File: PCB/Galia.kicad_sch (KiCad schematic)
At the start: 9 parts, among them J1 USB In, J2 USB, SW1 Bootsel, SW2 Reset, U2 TPD4E05U06

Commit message: Changed PTS645 LCSC part number
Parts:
- SW1, SW2: LCSC C285466 -> C285487
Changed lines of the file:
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@@
       (effects (font (size 1.27 1.27)) hide)
     )
-    (property "LCSC" "C285466" (at 134.62 27.94 0)
+    (property "LCSC" "C285487" (at 134.62 27.94 0)
       (effects (font (size 1.27 1.27)) hide)
     )
@@
       (effects (font (size 1.27 1.27)) hide)
     )
-    (property "LCSC" "C285466" (at 134.62 40.64 0)
+    (property "LCSC" "C285487" (at 134.62 40.64 0)
       (effects (font (size 1.27 1.27)) hide)
     )

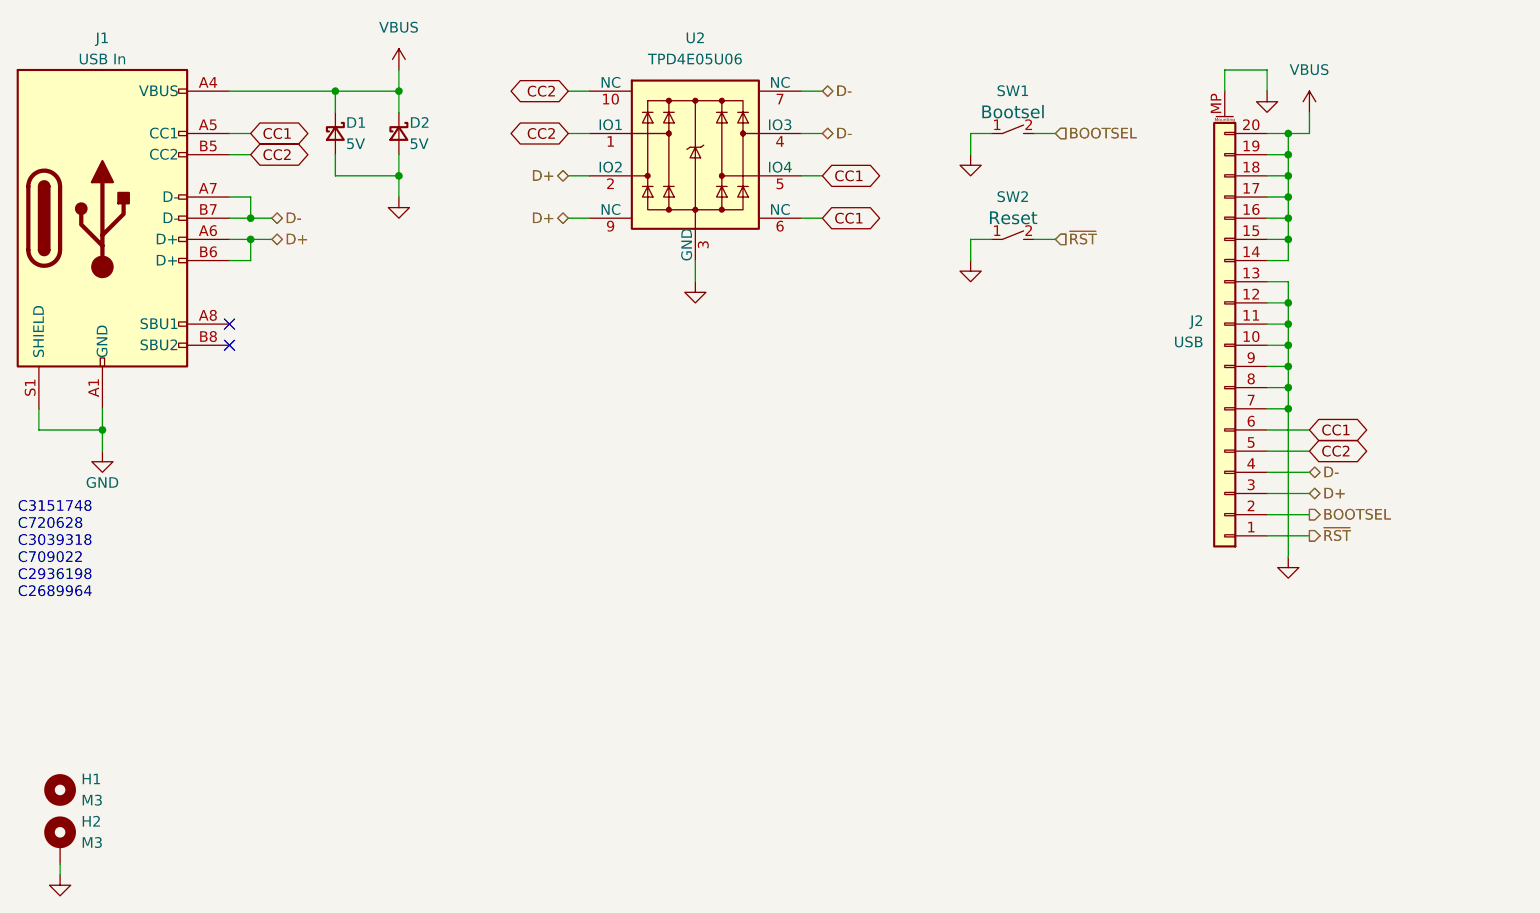
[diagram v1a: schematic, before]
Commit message: 17/07/2023 update
Changed 20 pin FFC connector to 14 pin JST SH connector. Repositioned components.
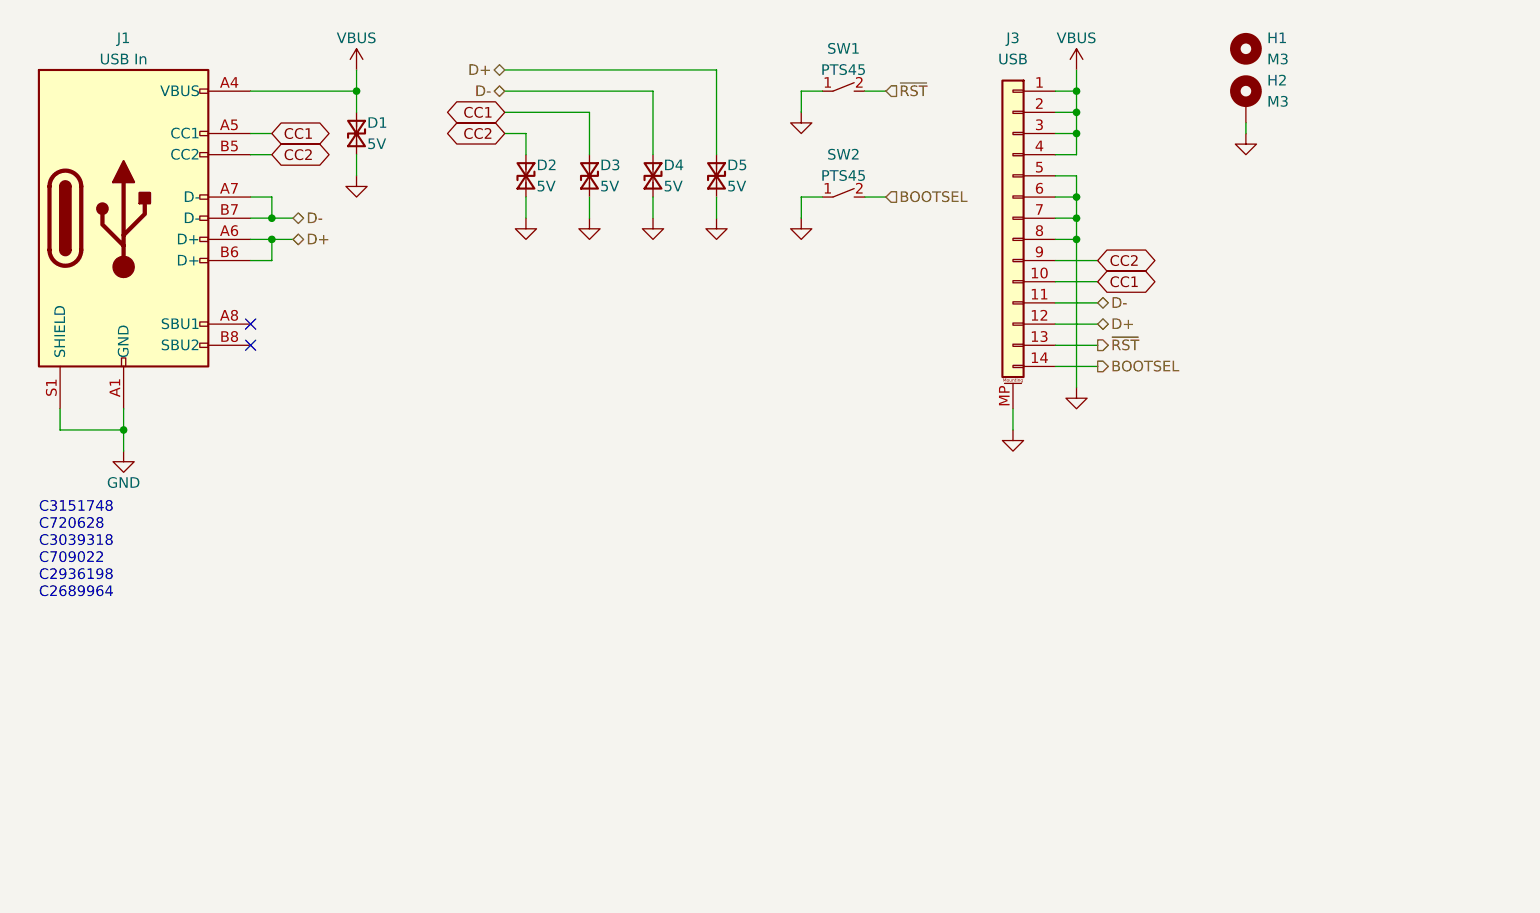
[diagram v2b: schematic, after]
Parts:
- removed D2: 5V, Diode_SMD:D_SOD-523, symbol Device:D_Schottky_Small
- removed J2: USB, Galia:HRS_FH34SRJ-20S-0.5SH(50), symbol Connector_Generic_MountingPin:Conn_01x20_MountingPin
- removed U2: TPD4E05U06, Galia:USON-10_2.5x1.0mm_P0.5mm, symbol Galia:TPD4E05U06
- added D2, D3, D4, D5: 5V, Galia:Texas_DPY0002A_0.6x1mm_P0.65mm, symbol Galia:D_TVS_Small
- added J3: USB, Galia:JST_SH_SM14B-SRSS-TB_1x14-1MP_P1.00mm_Horizontal, symbol Connector_Generic_MountingPin:Conn_01x14_MountingPin
- D1: symbol Device:D_Schottky_Small -> Galia:D_TVS_Small; LCSC C502546 -> C85708
- SW1: value Bootsel -> PTS45
- SW2: value Reset -> PTS45
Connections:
- net BOOTSEL: now also SW2.2 (B), J3.14 (Pin_14); no longer SW1.2 (B)
- net CC1: now also D3.1 (K), J3.10 (Pin_10)
- net CC2: now also D2.1 (K), J3.9 (Pin_9)
- net D+: now also D5.1 (K), J3.12 (Pin_12)
- net D-: now also D4.1 (K), J3.11 (Pin_11)
- net GND: now also D2.2 (A), D3.2 (A), D4.2 (A), D5.2 (A), J3.5 (Pin_5), J3.6 (Pin_6), J3.7 (Pin_7), J3.8 (Pin_8), J3.MP (MountPin)
- net VBUS: now also J3.1 (Pin_1), J3.2 (Pin_2), J3.3 (Pin_3), J3.4 (Pin_4)
- net ~{RST}: now also SW1.2 (B), J3.13 (Pin_13); no longer SW2.2 (B)
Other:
- moved on the sheet: H1, H2, J1, SW1, SW2

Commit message: 18/07/2023 update.
Changed JST connector back to 20 pin FFC. Centered connector.
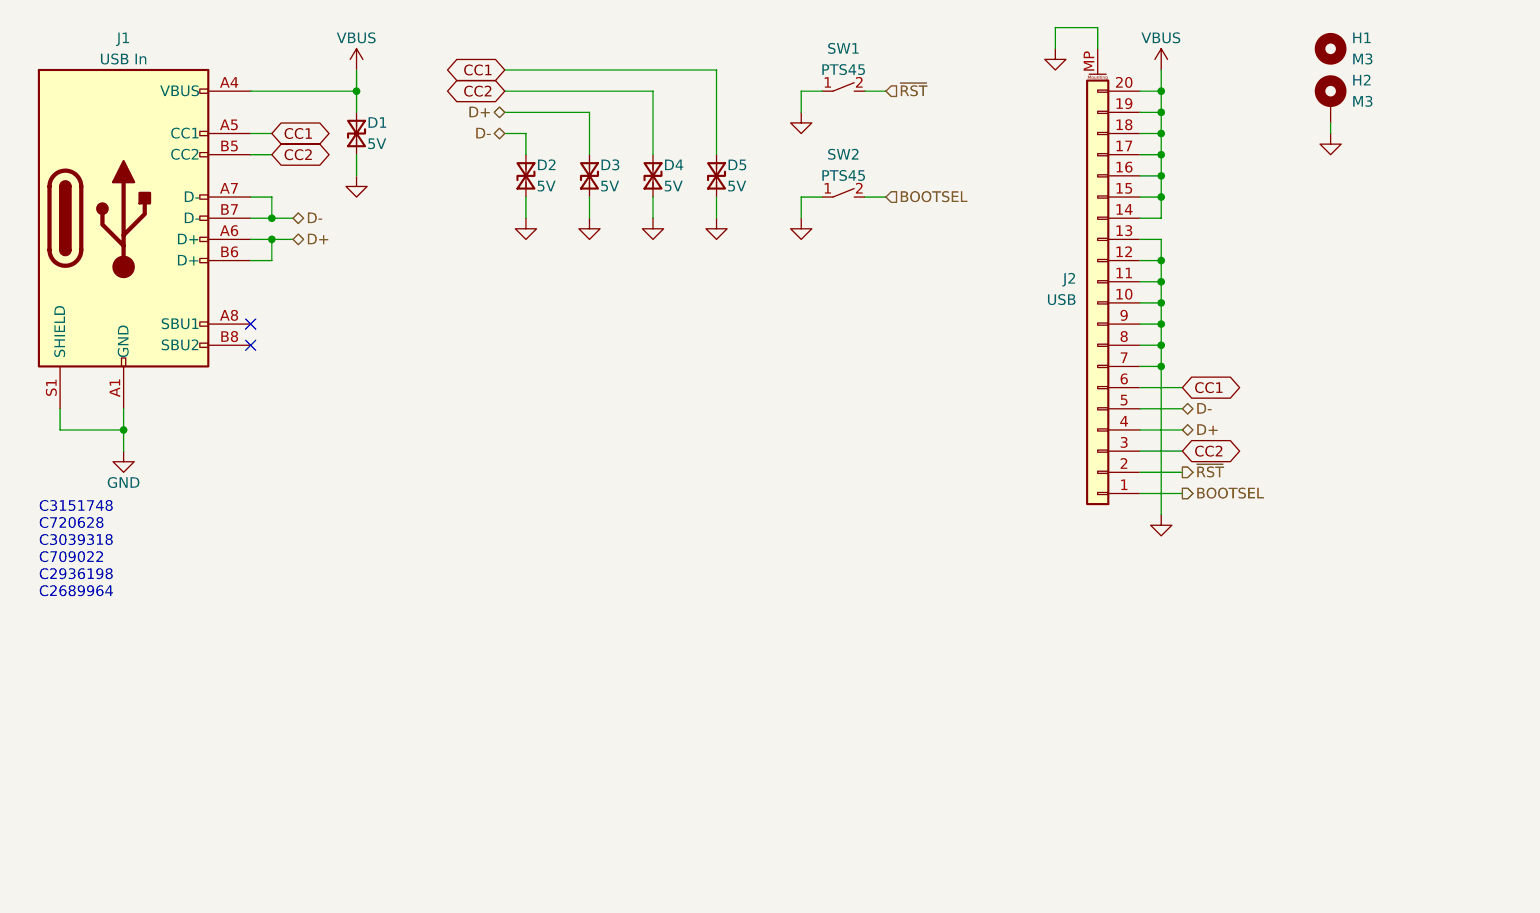
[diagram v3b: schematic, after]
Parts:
- removed J3: USB, Galia:JST_SH_SM14B-SRSS-TB_1x14-1MP_P1.00mm_Horizontal, symbol Connector_Generic_MountingPin:Conn_01x14_MountingPin
- added J2: USB, Galia:HRS_FH34SRJ-20S-0.5SH(50), symbol Connector_Generic_MountingPin:Conn_01x20_MountingPin
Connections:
- net BOOTSEL: now also J2.1 (Pin_1)
- net CC1: now also D5.1 (K), J2.6 (Pin_6); no longer D3.1 (K)
- net CC2: now also D4.1 (K), J2.3 (Pin_3); no longer D2.1 (K)
- net D+: now also D3.1 (K), J2.4 (Pin_4); no longer D5.1 (K)
- net D-: now also D2.1 (K), J2.5 (Pin_5); no longer D4.1 (K)
- net GND: now also J2.10 (Pin_10), J2.11 (Pin_11), J2.12 (Pin_12), J2.13 (Pin_13), J2.7 (Pin_7), J2.8 (Pin_8), J2.9 (Pin_9), J2.MP (MountPin)
- net VBUS: now also J2.14 (Pin_14), J2.15 (Pin_15), J2.16 (Pin_16), J2.17 (Pin_17), J2.18 (Pin_18), J2.19 (Pin_19), J2.20 (Pin_20)
- net ~{RST}: now also J2.2 (Pin_2)
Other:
- moved on the sheet: H1, H2

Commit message: Added LCSC part number.
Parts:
- J2: LCSC (none) -> C2802370
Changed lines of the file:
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@@
+      (effects (font (size 1.27 1.27)) hide)
+    )
+    (property "LCSC" "C2802370" (at 144.78 48.26 0)
       (effects (font (size 1.27 1.27)) hide)
     )

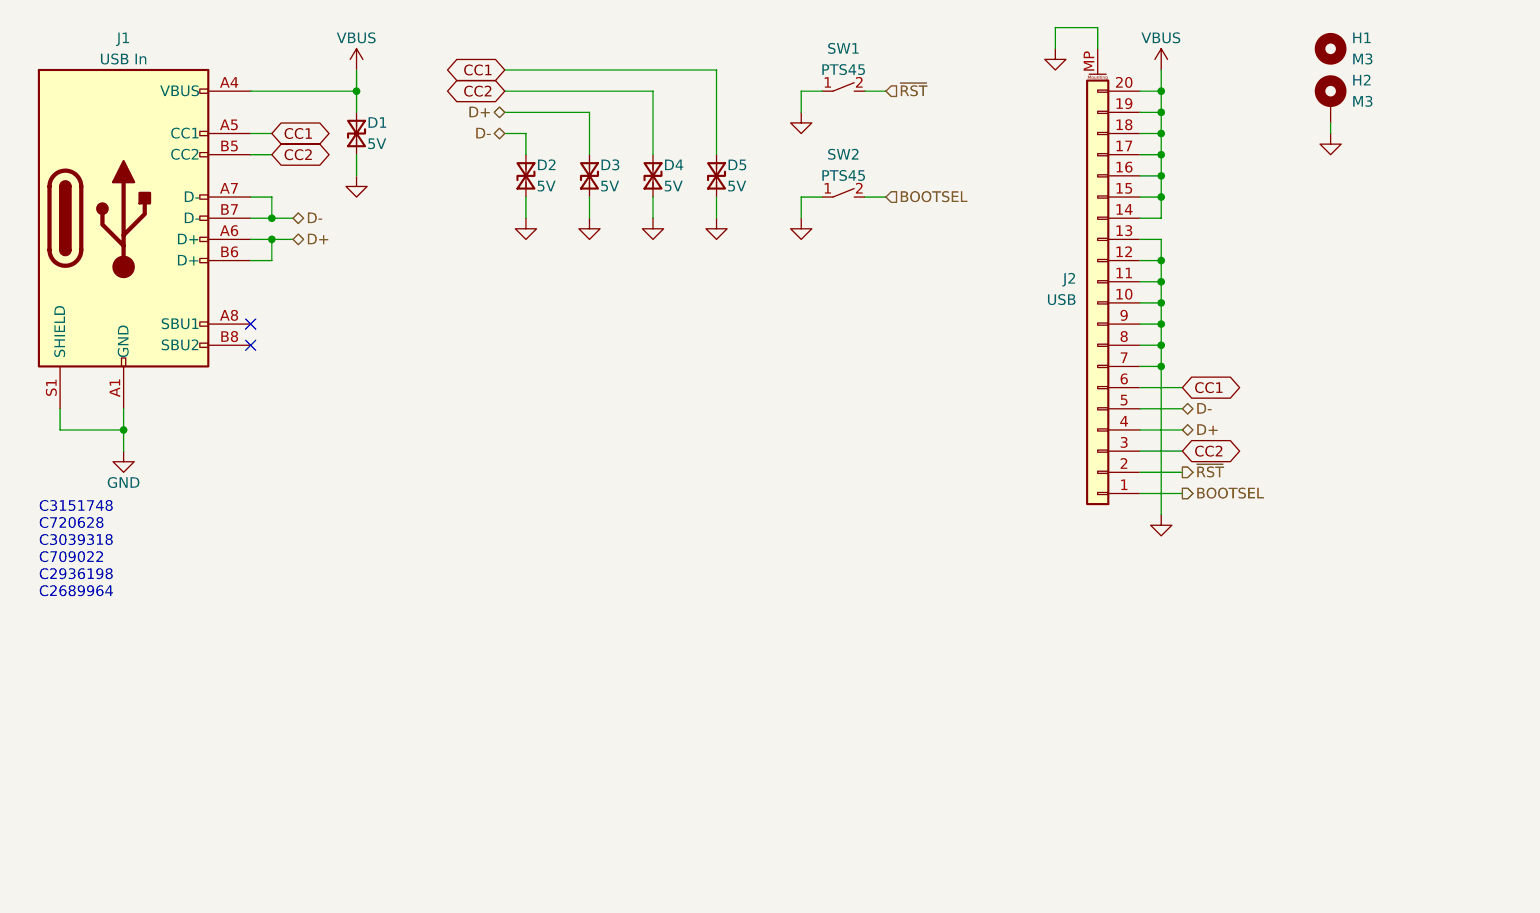
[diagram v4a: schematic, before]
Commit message: 21/07/2023 update.
Changed 20 pin FFC to 7 pin and 8 pin JST SH connector. Fixed orientation.
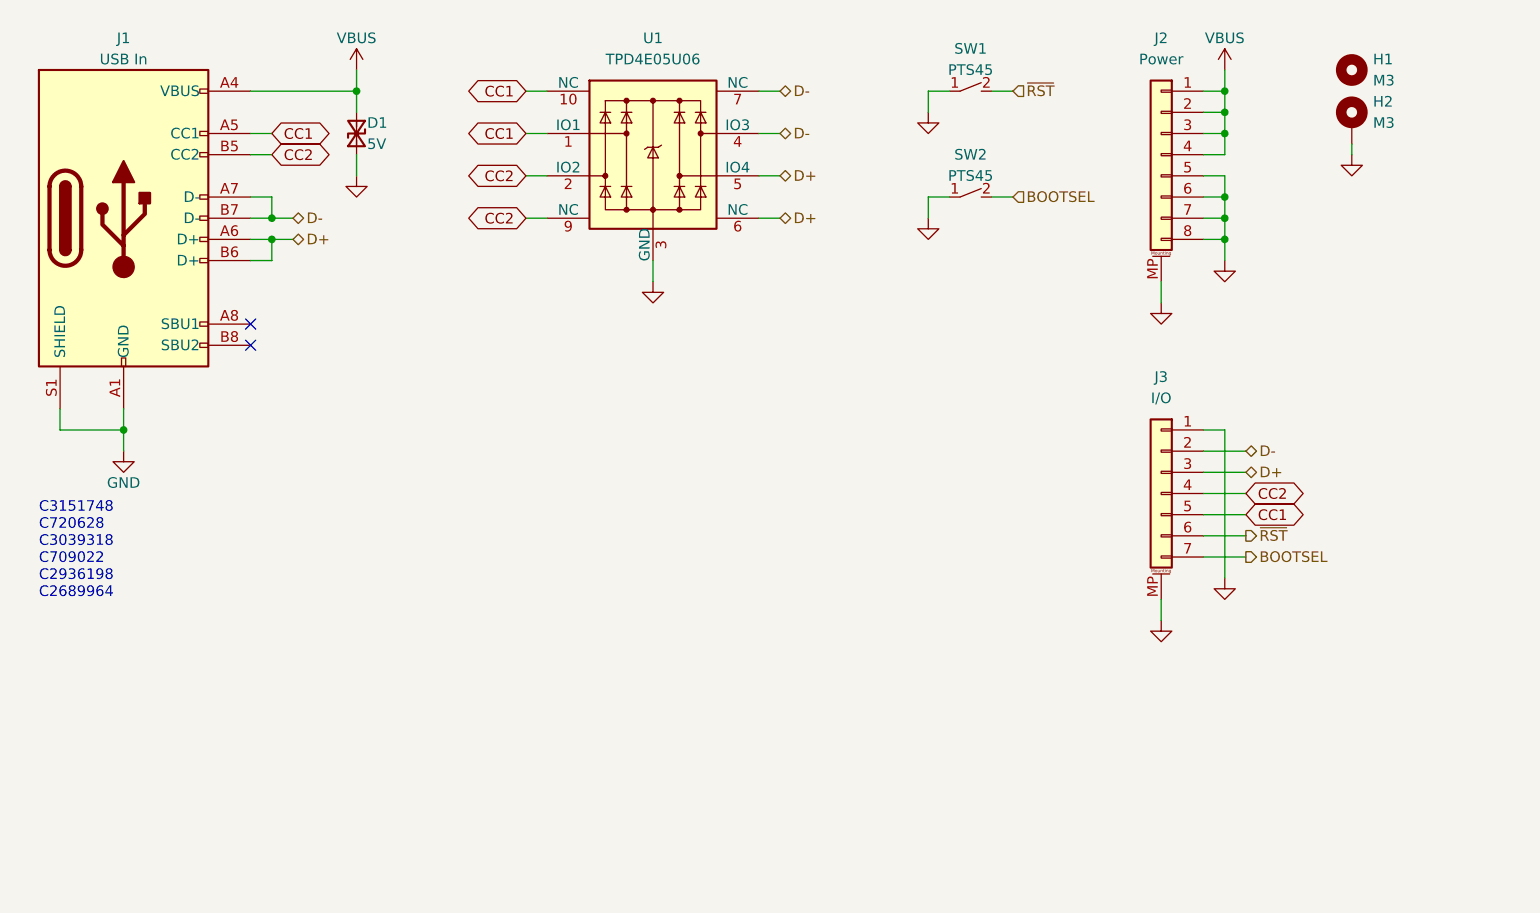
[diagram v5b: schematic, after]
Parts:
- removed D2, D3, D4, D5: 5V, Galia:Texas_DPY0002A_0.6x1mm_P0.65mm, symbol Galia:D_TVS_Small
- removed J2: USB, Galia:HRS_FH34SRJ-20S-0.5SH(50), symbol Connector_Generic_MountingPin:Conn_01x20_MountingPin
- added J2: Power, Galia:JST_SH_SM08B-SRSS-TB_1x08-1MP_P1.00mm_Horizontal, symbol Connector_Generic_MountingPin:Conn_01x08_MountingPin
- added J3: I/O, Galia:JST_SH_SM07B-SRSS-TB_1x07-1MP_P1.00mm_Horizontal, symbol Connector_Generic_MountingPin:Conn_01x07_MountingPin
- added U1: TPD4E05U06, Galia:USON-10_2.5x1.0mm_P0.5mm, symbol Galia:TPD4E05U06
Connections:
- net BOOTSEL: now also J3.7 (Pin_7)
- net CC1: now also J3.5 (Pin_5), U1.1 (IO1), U1.10 (NC)
- net CC2: now also J3.4 (Pin_4), U1.2 (IO2), U1.9 (NC)
- net D+: now also J3.3 (Pin_3), U1.5 (IO4), U1.6 (NC)
- net D-: now also J3.2 (Pin_2), U1.4 (IO3), U1.7 (NC)
- net GND: now also J2.5 (Pin_5), J2.6 (Pin_6), J2.7 (Pin_7), J2.8 (Pin_8), J2.MP (MountPin), J3.1 (Pin_1), J3.MP (MountPin), U1.3 (GND), U1.8 (GND)
- net VBUS: now also J2.1 (Pin_1), J2.2 (Pin_2), J2.3 (Pin_3), J2.4 (Pin_4)
- net ~{RST}: now also J3.6 (Pin_6)
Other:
- moved on the sheet: H1, H2, SW1, SW2

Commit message: 25/07/2023 update
Changed 8 pin JST SH connector to 6 pin. Changed orientation of SH connectors for easier routing of wires. Added Ariamelon logo. Added PCB cutouts to allow for buttons to be snapped off.
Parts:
- removed J2: Power, Galia:JST_SH_SM08B-SRSS-TB_1x08-1MP_P1.00mm_Horizontal, symbol Connector_Generic_MountingPin:Conn_01x08_MountingPin
- added A1: Ariamelon Logo, Galia:Ariamelon_Logo_Mask, symbol Mechanical:Fiducial
- added J2: Power, Galia:JST_SH_SM06B-SRSS-TB_1x06-1MP_P1.00mm_Horizontal, symbol Connector_Generic_MountingPin:Conn_01x06_MountingPin
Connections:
- net BOOTSEL: now also J3.1 (Pin_1); no longer J3.7 (Pin_7)
- net CC1: now also J3.3 (Pin_3); no longer J3.5 (Pin_5)
- net D+: now also J3.5 (Pin_5); no longer J3.3 (Pin_3)
- net D-: now also J3.6 (Pin_6); no longer J3.2 (Pin_2)
- net GND: now also J3.7 (Pin_7), J2.1 (Pin_1), J2.2 (Pin_2), J2.3 (Pin_3), J2.MP (MountPin); no longer J3.1 (Pin_1)
- net VBUS: now also J2.4 (Pin_4), J2.5 (Pin_5), J2.6 (Pin_6)
- net ~{RST}: now also J3.2 (Pin_2); no longer J3.6 (Pin_6)
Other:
- moved on the sheet: J3
